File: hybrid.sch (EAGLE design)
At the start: 124 parts, among them IC1 TL071P, IC2 TL071P, IC3 LM317MABT, IC4 LM317MABT, J1 RCJ-21XXMILL, J2 NRJ3HF-1, J3 703W-00/54, Q1 BC560KINKED, Q10 BC560KINKED, Q11 BC560KINKED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

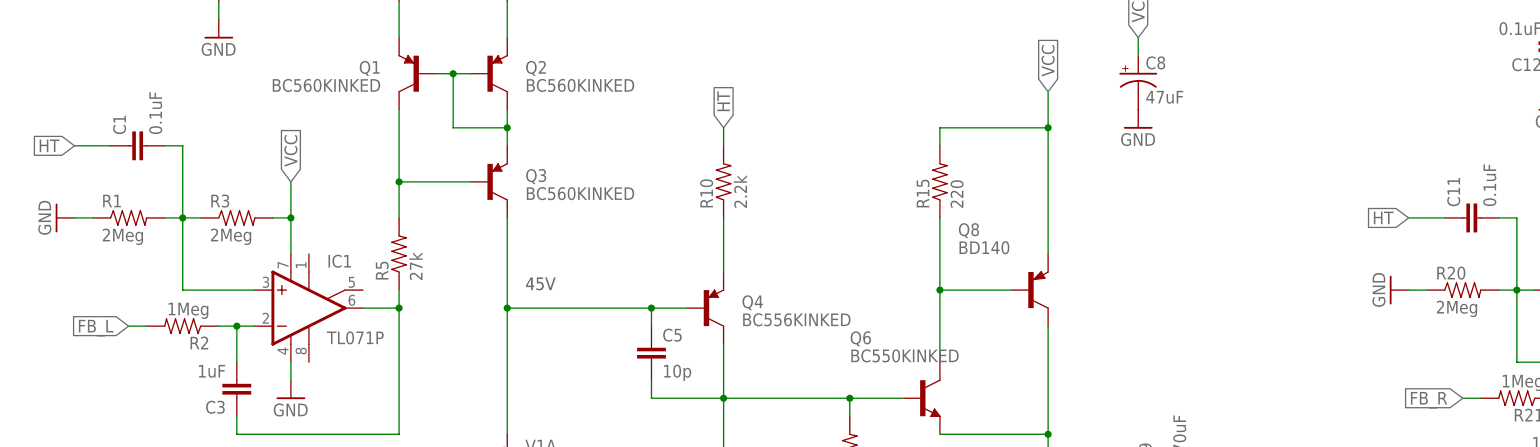
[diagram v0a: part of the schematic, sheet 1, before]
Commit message: Back to gain stage with uncompensated PSN
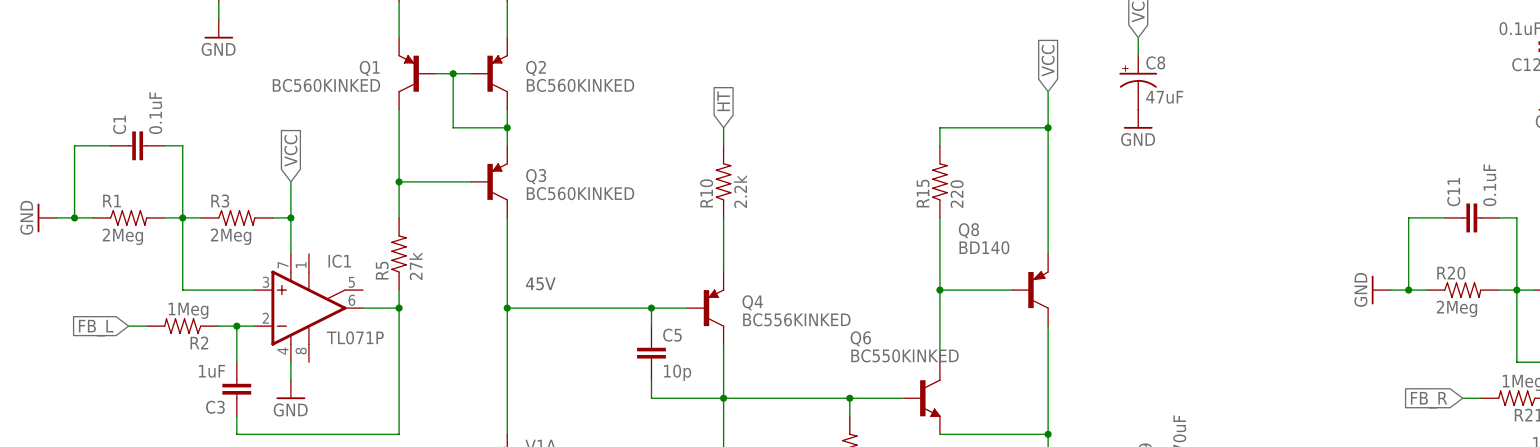
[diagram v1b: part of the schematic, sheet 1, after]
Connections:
- net GND: now also C1.1, C11.1
- net HT: no longer C1.1, C11.1
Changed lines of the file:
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@@
 <instance part="R3" gate="G$1" x="35.56" y="187.96"/>
 <instance part="R1" gate="G$1" x="20.32" y="187.96"/>
-<instance part="GND1" gate="1" x="10.16" y="187.96" rot="R270"/>
+<instance part="GND1" gate="1" x="7.62" y="187.96" rot="R270"/>
 <instance part="C1" gate="G$1" x="22.86" y="198.12" rot="R90"/>
 <instance part="C2" gate="G$1" x="33.02" y="223.52" rot="R180"/>
@@
 <instance part="R22" gate="G$1" x="223.52" y="177.8"/>
 <instance part="R20" gate="G$1" x="208.28" y="177.8"/>
-<instance part="GND16" gate="1" x="198.12" y="177.8" rot="R270"/>
+<instance part="GND16" gate="1" x="195.58" y="177.8" rot="R270"/>
 <instance part="C11" gate="G$1" x="210.82" y="187.96" rot="R90"/>
 <instance part="C12" gate="G$1" x="220.98" y="213.36" rot="R180"/>
@@
 <wire x1="15.24" y1="187.96" x2="12.7" y2="187.96" width="0.1524" layer="91"/>
 <pinref part="GND1" gate="1" pin="GND"/>
+<pinref part="C1" gate="G$1" pin="1"/>
+<wire x1="12.7" y1="187.96" x2="10.16" y2="187.96" width="0.1524" layer="91"/>
+<wire x1="17.78" y1="198.12" x2="12.7" y2="198.12" width="0.1524" layer="91"/>
+<wire x1="12.7" y1="198.12" x2="12.7" y2="187.96" width="0.1524" layer="91"/>
+<junction x="12.7" y="187.96"/>
 </segment>
 <segment>
@@
 <wire x1="203.2" y1="177.8" x2="200.66" y2="177.8" width="0.1524" layer="91"/>
 <pinref part="GND16" gate="1" pin="GND"/>
+<pinref part="C11" gate="G$1" pin="1"/>
+<wire x1="200.66" y1="177.8" x2="198.12" y2="177.8" width="0.1524" layer="91"/>
+<wire x1="205.74" y1="187.96" x2="200.66" y2="187.96" width="0.1524" layer="91"/>
+<wire x1="200.66" y1="187.96" x2="200.66" y2="177.8" width="0.1524" layer="91"/>
+<junction x="200.66" y="177.8"/>
 </segment>
 <segment>
@@
 <pinref part="R23" gate="G$1" pin="2"/>
 </segment>
-<segment>
-<pinref part="C1" gate="G$1" pin="1"/>
-<wire x1="17.78" y1="198.12" x2="12.7" y2="198.12" width="0.1524" layer="91"/>
-<label x="12.7" y="198.12" size="1.778" layer="95" rot="R180" xref="yes"/>
-</segment>
-<segment>
-<pinref part="C11" gate="G$1" pin="1"/>
-<wire x1="205.74" y1="187.96" x2="200.66" y2="187.96" width="0.1524" layer="91"/>
-<label x="200.66" y="187.96" size="1.778" layer="95" rot="R180" xref="yes"/>
-</segment>
-</net>
+</net>

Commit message: Horizontal version
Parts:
- removed H1: MOUNT-HOLE3.2, holes:MOUNT-HOLE3.2
- V1: value 6DJ8 -> (none); device my-tubes:6DJ8-P21MM-BASE -> my-tubes:6DJ8-P-HORIZONTAL
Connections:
- net +6.3FIL: now also V1HEATER.H1; no longer V1".H1
- net FGND: now also V1HEATER.H2; no longer V1".H3
- net GND: now also V1GNDPLANE.GND
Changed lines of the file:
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@@
 </classes>
 <parts>
-<part name="V1" library="my-tubes" deviceset="6DJ8-P" device="21MM-BASE" value="6DJ8"/>
 <part name="Q2" library="my-tran" deviceset="BC560" device="KINKED"/>
 <part name="R8" library="SparkFun-Resistors" deviceset="RESISTOR" device="PTH-1/4W" value="820"/>
@@
 <part name="GND36" library="SparkFun-Aesthetics" deviceset="GND" device=""/>
 <part name="GND37" library="SparkFun-Aesthetics" deviceset="GND" device=""/>
-<part name="H1" library="holes" deviceset="MOUNT-HOLE" device="3.2"/>
 <part name="H2" library="holes" deviceset="MOUNT-HOLE" device="3.2"/>
 <part name="H3" library="holes" deviceset="MOUNT-HOLE" device="3.2"/>
@@
 <part name="GND6" library="SparkFun-Aesthetics" deviceset="GND" device=""/>
 <part name="U$1" library="my-logo" deviceset="ACRIDA-LOGO" device=""/>
+<part name="V1" library="my-tubes" deviceset="6DJ8-P-HORIZONTAL" device=""/>
+<part name="GND38" library="SparkFun-Aesthetics" deviceset="GND" device=""/>
 </parts>
 <sheets>
@@
 </plain>
 <instances>
-<instance part="V1" gate="A" x="73.66" y="147.32"/>
-<instance part="V1" gate="B" x="261.62" y="137.16"/>
-<instance part="V1" gate="&quot;" x="246.38" y="35.56"/>
 <instance part="Q2" gate="G$1" x="71.12" y="208.28"/>
 <instance part="R8" gate="G$1" x="73.66" y="124.46" rot="R90"/>
@@
 <instance part="GND36" gate="1" x="27.94" y="22.86"/>
 <instance part="GND37" gate="1" x="71.12" y="22.86"/>
-<instance part="H1" gate="G$1" x="289.56" y="45.72"/>
 <instance part="H2" gate="G$1" x="317.5" y="45.72"/>
 <instance part="H3" gate="G$1" x="345.44" y="45.72"/>
@@
 <instance part="GND2" gate="1" x="284.48" y="58.42" rot="R270"/>
 <instance part="H5" gate="G$1" x="345.44" y="55.88"/>
+<instance part="V1" gate="A" x="73.66" y="147.32"/>
+<instance part="V1" gate="B" x="261.62" y="137.16"/>
+<instance part="V1" gate="GNDPLANE" x="223.52" y="109.22"/>
+<instance part="V1" gate="HEATER" x="246.38" y="35.56"/>
+<instance part="GND38" gate="1" x="223.52" y="93.98"/>
 </instances>
 <busses>
@@
 <net name="PL_L" class="0">
 <segment>
-<pinref part="V1" gate="A" pin="TA"/>
 <wire x1="73.66" y1="157.48" x2="73.66" y2="175.26" width="0.1524" layer="91"/>
 <pinref part="Q4" gate="G$1" pin="B"/>
@@
 <junction x="93.98" y="175.26"/>
 <pinref part="Q3" gate="G$1" pin="C"/>
+<pinref part="V1" gate="A" pin="TA"/>
 </segment>
 </net>
@@
 <pinref part="GND2" gate="1" pin="GND"/>
 </segment>
+<segment>
+<pinref part="V1" gate="GNDPLANE" pin="GND"/>
+<pinref part="GND38" gate="1" pin="GND"/>
+<wire x1="223.52" y1="104.14" x2="223.52" y2="96.52" width="0.1524" layer="91"/>
+</segment>
 </net>
 <net name="CAT_L" class="0">
 <segment>
-<pinref part="V1" gate="A" pin="TK"/>
 <pinref part="R8" gate="G$1" pin="2"/>
 <wire x1="73.66" y1="137.16" x2="73.66" y2="132.08" width="0.1524" layer="91"/>
@@
 <wire x1="81.28" y1="132.08" x2="73.66" y2="132.08" width="0.1524" layer="91"/>
 <junction x="73.66" y="132.08"/>
+<pinref part="V1" gate="A" pin="TK"/>
 </segment>
 </net>
@@
 <pinref part="Q13" gate="G$1" pin="B"/>
 <wire x1="287.02" y1="165.1" x2="281.94" y2="165.1" width="0.1524" layer="91"/>
-<pinref part="V1" gate="B" pin="TA"/>
 <pinref part="C15" gate="G$1" pin="1"/>
 <wire x1="281.94" y1="165.1" x2="261.62" y2="165.1" width="0.1524" layer="91"/>
 <wire x1="281.94" y1="162.56" x2="281.94" y2="165.1" width="0.1524" layer="91"/>
 <junction x="281.94" y="165.1"/>
-</segment>
-<segment>
-<wire x1="261.62" y1="147.32" x2="261.62" y2="165.1" width="0.1524" layer="91"/>
+<pinref part="V1" gate="B" pin="TA"/>
+</segment>
+<segment>
 <wire x1="261.62" y1="165.1" x2="261.62" y2="177.8" width="0.1524" layer="91"/>
-<junction x="261.62" y="165.1"/>
 <wire x1="281.94" y1="165.1" x2="261.62" y2="165.1" width="0.1524" layer="91"/>
 <pinref part="Q12" gate="G$1" pin="C"/>
@@
 <net name="+6.3FIL" class="2">
 <segment>
-<pinref part="V1" gate="&quot;" pin="H1"/>
 <wire x1="246.38" y1="48.26" x2="246.38" y2="45.72" width="0.1524" layer="91"/>
 <label x="246.38" y="48.26" size="1.778" layer="95" rot="R90" xref="yes"/>
+<pinref part="V1" gate="HEATER" pin="H1"/>
 </segment>
 </net>
 <net name="G_L" class="0">
 <segment>
-<pinref part="V1" gate="A" pin="TG"/>
 <pinref part="C4" gate="G$1" pin="2"/>
 <wire x1="63.5" y1="147.32" x2="60.96" y2="147.32" width="0.1524" layer="91"/>
@@
 <wire x1="60.96" y1="137.16" x2="60.96" y2="147.32" width="0.1524" layer="91"/>
 <junction x="60.96" y="147.32"/>
+<pinref part="V1" gate="A" pin="TG"/>
 </segment>
 </net>
@@
 <segment>
 <pinref part="C14" gate="G$1" pin="2"/>
-<pinref part="V1" gate="B" pin="TG"/>
 <wire x1="243.84" y1="137.16" x2="248.92" y2="137.16" width="0.1524" layer="91"/>
 <pinref part="R25" gate="G$1" pin="2"/>
@@
 <wire x1="248.92" y1="127" x2="248.92" y2="137.16" width="0.1524" layer="91"/>
 <junction x="248.92" y="137.16"/>
+<pinref part="V1" gate="B" pin="TG"/>
 </segment>
 </net>
@@
 <net name="FGND" class="2">
 <segment>
-<pinref part="V1" gate="&quot;" pin="H3"/>
 <wire x1="246.38" y1="22.86" x2="246.38" y2="25.4" width="0.1524" layer="91"/>
 <label x="246.38" y="22.86" size="1.778" layer="95" rot="R270" xref="yes"/>
-</segment>
-</net>
+<pinref part="V1" gate="HEATER" pin="H2"/>
+</segment>
+</net>

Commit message: Snap in cap
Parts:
- removed C25: 2200uF, my-cap:CAP_POLPTH-18/7.5
- C23: value 2200uF -> 4700uF; device my-cap:CAP_POLPTH-18/7.5 -> my-cap:CAP_POLSNAPIN-30/10
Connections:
- net +LV: no longer C25.+
- net GND: no longer C25.-
